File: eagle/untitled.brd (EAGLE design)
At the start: 50 x 50 mm, 58 parts, among them J1 JTAG, Q1 16MHz, U1 MMA3202KEG

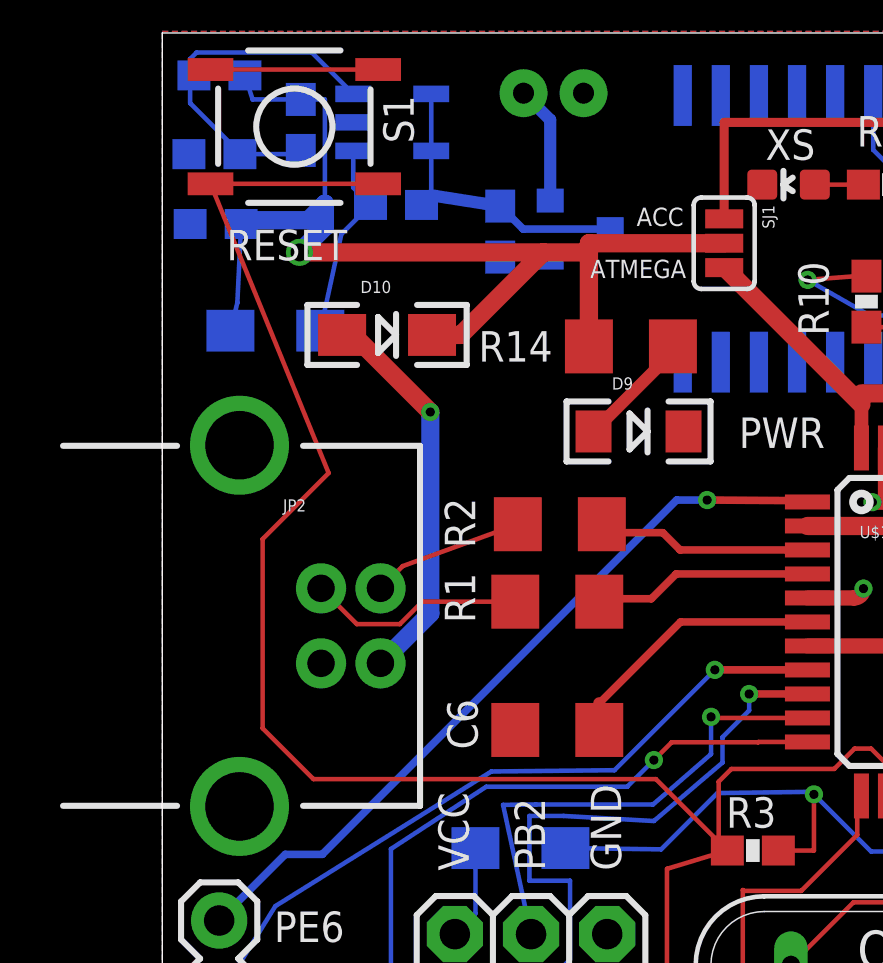
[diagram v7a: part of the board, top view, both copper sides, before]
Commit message: Reroute reset signal.
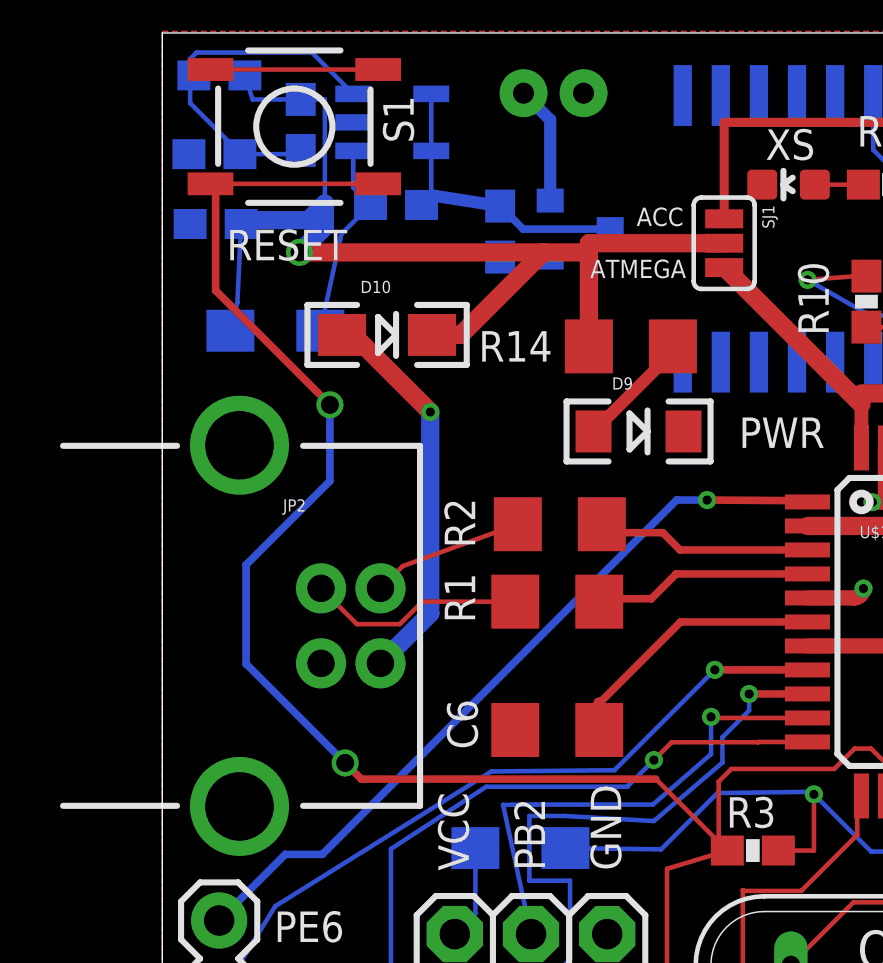
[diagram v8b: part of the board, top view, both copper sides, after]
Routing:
- net N$17: track 60.7 -> 61.1 mm, vias 0 -> 2
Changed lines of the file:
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@@
 <grid distance="100" unitdist="mil" unit="mil" style="lines" multiple="1" display="yes" altdistance="10" altunitdist="mil" altunit="mil"/>
 <layers>
-<layer number="1" name="Top" color="4" fill="1" visible="no" active="yes"/>
-<layer number="16" name="Bottom" color="1" fill="1" visible="yes" active="yes"/>
+<layer number="1" name="Top" color="4" fill="1" visible="yes" active="yes"/>
+<layer number="16" name="Bottom" color="1" fill="1" visible="no" active="yes"/>
 <layer number="17" name="Pads" color="2" fill="1" visible="yes" active="yes"/>
 <layer number="18" name="Vias" color="2" fill="1" visible="yes" active="yes"/>
 <layer number="19" name="Unrouted" color="2" fill="1" visible="yes" active="yes"/>
-<layer number="20" name="Dimension" color="15" fill="1" visible="no" active="yes"/>
-<layer number="21" name="tPlace" color="7" fill="1" visible="no" active="yes"/>
-<layer number="22" name="bPlace" color="15" fill="1" visible="yes" active="yes"/>
-<layer number="23" name="tOrigins" color="15" fill="1" visible="no" active="yes"/>
-<layer number="24" name="bOrigins" color="15" fill="1" visible="yes" active="yes"/>
-<layer number="25" name="tNames" color="7" fill="1" visible="no" active="yes"/>
-<layer number="26" name="bNames" color="7" fill="1" visible="yes" active="yes"/>
+<layer number="20" name="Dimension" color="15" fill="1" visible="yes" active="yes"/>
+<layer number="21" name="tPlace" color="7" fill="1" visible="yes" active="yes"/>
+<layer number="22" name="bPlace" color="15" fill="1" visible="no" active="yes"/>
+<layer number="23" name="tOrigins" color="15" fill="1" visible="yes" active="yes"/>
+<layer number="24" name="bOrigins" color="15" fill="1" visible="no" active="yes"/>
+<layer number="25" name="tNames" color="7" fill="1" visible="yes" active="yes"/>
+<layer number="26" name="bNames" color="7" fill="1" visible="no" active="yes"/>
 <layer number="27" name="tValues" color="7" fill="1" visible="no" active="yes"/>
 <layer number="28" name="bValues" color="7" fill="1" visible="no" active="yes"/>
 <layer number="29" name="tStop" color="7" fill="3" visible="no" active="yes"/>
-<layer number="30" name="bStop" color="7" fill="6" visible="yes" active="yes"/>
+<layer number="30" name="bStop" color="7" fill="6" visible="no" active="yes"/>
 <layer number="31" name="tCream" color="7" fill="4" visible="no" active="yes"/>
 <layer number="32" name="bCream" color="7" fill="5" visible="no" active="yes"/>
@@
 <layer number="49" name="Reference" color="7" fill="1" visible="no" active="yes"/>
 <layer number="50" name="dxf" color="7" fill="1" visible="no" active="no"/>
-<layer number="51" name="tDocu" color="11" fill="7" visible="no" active="yes"/>
+<layer number="51" name="tDocu" color="11" fill="7" visible="yes" active="yes"/>
 <layer number="52" name="bDocu" color="7" fill="1" visible="no" active="yes"/>
 <layer number="53" name="tGND_GNDA" color="7" fill="9" visible="no" active="no"/>
@@
 <wire x1="19.053709375" y1="51.470290625" x2="19.343" y2="51.181" width="0.1524" layer="1"/>
 <wire x1="19.343" y1="51.181" x2="16.96131875" y2="53.56268125" width="0.1524" layer="1"/>
-<wire x1="16.96131875" y1="53.56268125" x2="5.546675" y2="53.56268125" width="0.1524" layer="1"/>
-<wire x1="5.546675" y1="53.56268125" x2="3.853003125" y2="55.256353125" width="0.1524" layer="1"/>
-<wire x1="3.853003125" y1="55.256353125" x2="3.853003125" y2="61.56528125" width="0.1524" layer="1"/>
-<wire x1="3.853003125" y1="61.56528125" x2="6.052796875" y2="63.765075" width="0.1524" layer="1"/>
-<wire x1="6.052796875" y1="63.765075" x2="2.115009375" y2="73.406" width="0.1524" layer="1"/>
+<wire x1="16.96131875" y1="53.56268125" x2="7.14331875" y2="53.56268125" width="0.254" layer="1"/>
+<wire x1="7.14331875" y1="53.56268125" x2="6.604" y2="54.102" width="0.254" layer="1"/>
+<via x="6.604" y="54.102" extent="1-16" drill="0.6"/>
+<wire x1="6.604" y1="54.102" x2="3.302" y2="57.404" width="0.254" layer="16"/>
+<wire x1="3.302" y1="57.404" x2="3.302" y2="60.706" width="0.254" layer="16"/>
+<wire x1="3.302" y1="60.706" x2="6.096" y2="63.5" width="0.254" layer="16"/>
+<wire x1="2.286" y1="69.85" x2="2.286" y2="73.235009375" width="0.254" layer="1"/>
+<wire x1="2.286" y1="73.235009375" x2="2.115009375" y2="73.406" width="0.254" layer="1"/>
+<wire x1="6.096" y1="63.5" x2="6.096" y2="66.04" width="0.254" layer="16"/>
+<via x="6.096" y="66.04" extent="1-16" drill="0.6"/>
+<wire x1="6.096" y1="66.04" x2="2.286" y2="69.85" width="0.254" layer="1"/>
 </signal>
 <signal name="Y">
